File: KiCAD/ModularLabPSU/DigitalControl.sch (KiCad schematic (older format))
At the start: 40 parts, among them CON1 AVR-ISP-6, IC1 ATMEGA328P-A, J1 USB_MINI_B_OTG, U2 AD7705BRUZ, U3 AD780BRZ, U4 AD5689, U5 ADUM1201ARZ-RL7, U6 MCP2200, U7 LT1639, X1 20MHz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

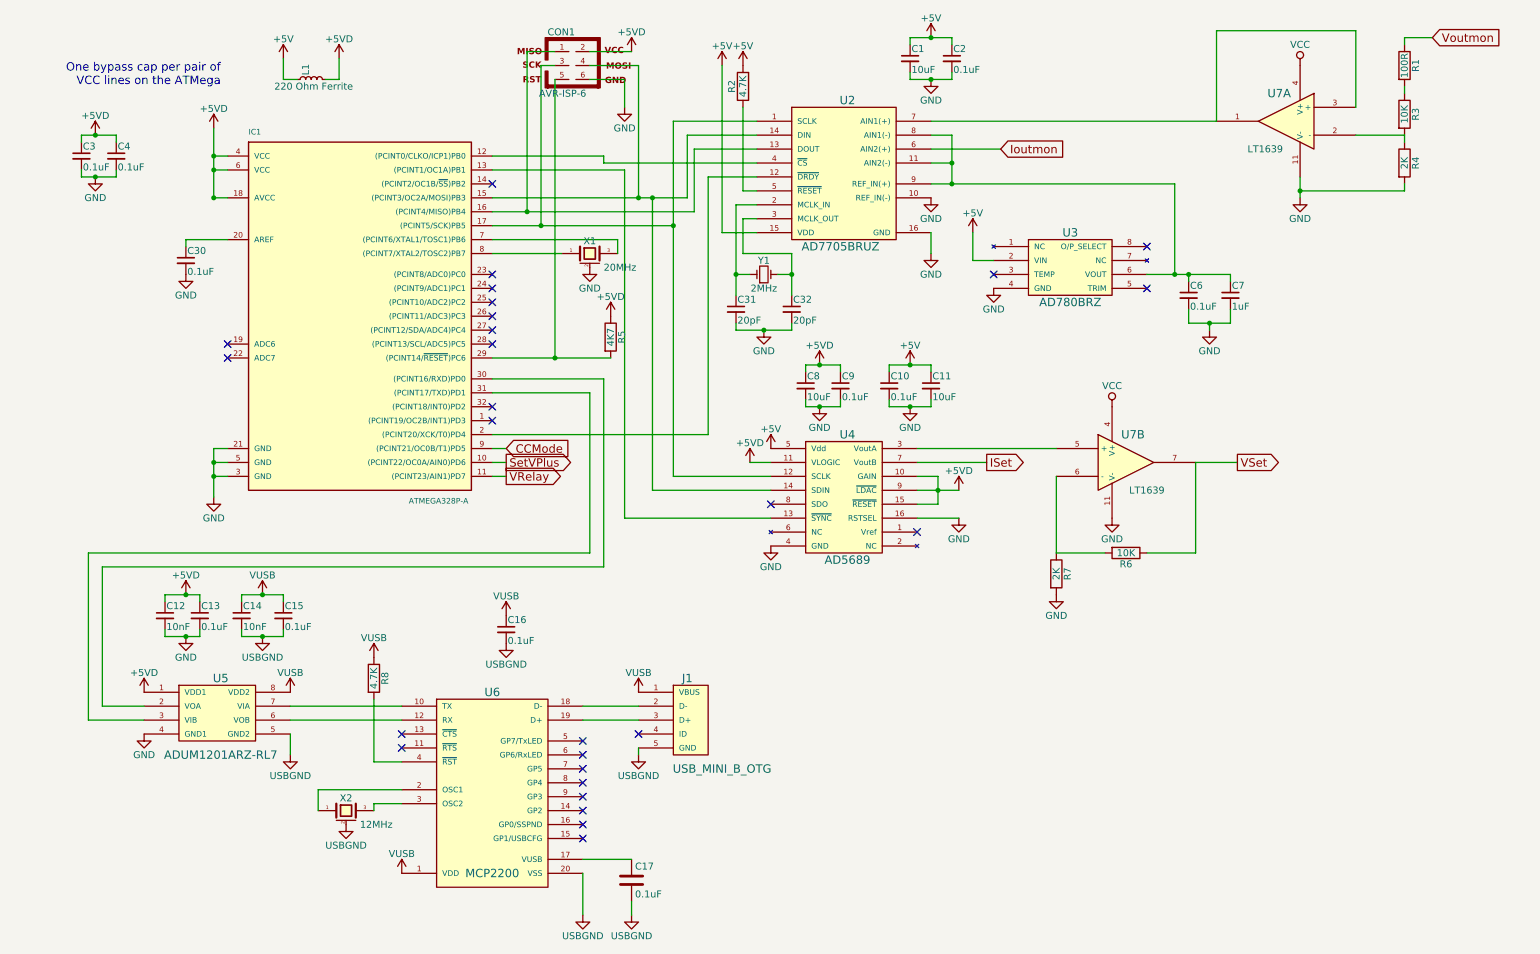
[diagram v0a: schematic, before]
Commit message: Started re-design of PCB. Schematic changes from testing first board and started developing new layout
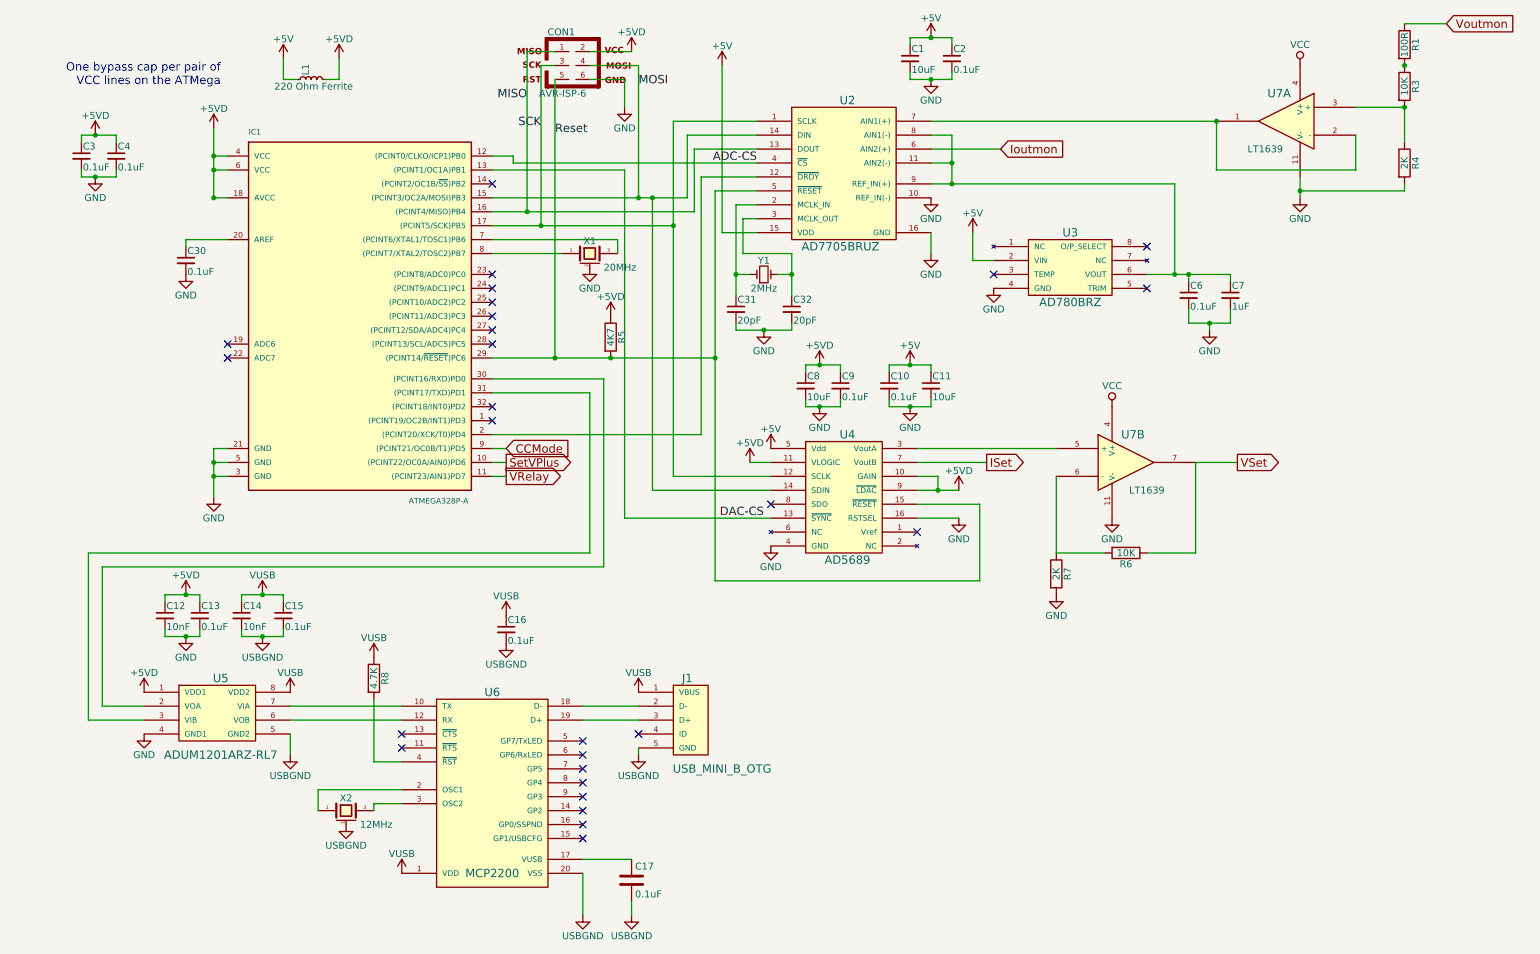
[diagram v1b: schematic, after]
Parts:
- removed R2: 4.7K, Resistors_SMD:R_0805_HandSoldering, symbol R
- U2: footprint Housings_SSOP:TSSOP-16_4.4x5mm_Pitch0.65mm -> Housings_SOIC:SOIC-16_7.5x10.3mm_Pitch1.27mm
- U6: footprint SMD_Packages:SSOP-20 -> Housings_SSOP:SSOP-20_5.3x7.2mm_Pitch0.65mm
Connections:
- net +5VD: no longer U4.15 (~RESET)
- net SCK: now reaches CON1.3, IC1.17 ((PCINT5/SCK)PB5), U2.1 (SCLK), U4.12 (SCLK)
- net MISO: now reaches CON1.1, IC1.16 ((PCINT4/MISO)PB4), U2.13 (DOUT)
- net MOSI: now reaches CON1.4, IC1.15 ((PCINT3/OC2A/MOSI)PB3), U2.14 (DIN), U4.14 (SDIN)
- net ADC-CS: now reaches IC1.12 ((PCINT0/CLKO/ICP1)PB0), U2.4 (~CS)
- net Reset: now reaches U2.5 (~RESET)
- net Reset: now also CON1.5, IC1.29 ((PCINT14/~RESET~)PC6), R5.2, U4.15 (~RESET)
- net at U2.7 (AIN1(+)), U7.1: now also U7.2 (-); no longer U7.3 (+)
- net at R3.2, R4.1: now also U7.3 (+); no longer U7.2 (-)
- net DAC-CS: now reaches IC1.13 ((PCINT1/OC1A)PB1), U4.13 (~SYNC)
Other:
- moved on the sheet: R1, R3

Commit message: Missed a couple of stars on precision resistors
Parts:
- R1: value 100R -> 100R*
- R3, R6: value 10K -> 10K*
- R4, R7: value 2K -> 2K*
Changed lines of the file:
@@
 P 10400 700
 F 0 "R1" V 10480 700 50  0000 C CNN
-F 1 "100R" V 10400 700 50  0000 C CNN
+F 1 "100R*" V 10400 700 50  0000 C CNN
 F 2 "Resistors_SMD:R_0805_HandSoldering" V 10330 700 30  0001 C CNN
 F 3 "" H 10400 700 30  0000 C CNN
@@
 P 10400 1000
 F 0 "R3" V 10480 1000 50  0000 C CNN
-F 1 "10K" V 10400 1000 50  0000 C CNN
+F 1 "10K*" V 10400 1000 50  0000 C CNN
 F 2 "Resistors_SMD:R_0805_HandSoldering" V 10330 1000 30  0001 C CNN
 F 3 "" H 10400 1000 30  0000 C CNN
@@
 P 10400 1550
 F 0 "R4" V 10480 1550 50  0000 C CNN
-F 1 "2K" V 10400 1550 50  0000 C CNN
+F 1 "2K*" V 10400 1550 50  0000 C CNN
 F 2 "Resistors_SMD:R_0805_HandSoldering" V 10330 1550 30  0001 C CNN
 F 3 "" H 10400 1550 30  0000 C CNN
@@
 P 8400 4350
 F 0 "R6" V 8480 4350 50  0000 C CNN
-F 1 "10K" V 8400 4350 50  0000 C CNN
+F 1 "10K*" V 8400 4350 50  0000 C CNN
 F 2 "Resistors_SMD:R_0805_HandSoldering" V 8330 4350 30  0001 C CNN
 F 3 "" H 8400 4350 30  0000 C CNN
@@
 P 7900 4500
 F 0 "R7" V 7980 4500 50  0000 C CNN
-F 1 "2K" V 7900 4500 50  0000 C CNN
+F 1 "2K*" V 7900 4500 50  0000 C CNN
 F 2 "Resistors_SMD:R_0805_HandSoldering" V 7830 4500 30  0001 C CNN
 F 3 "" H 7900 4500 30  0000 C CNN
